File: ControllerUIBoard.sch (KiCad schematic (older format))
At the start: 27 parts, among them J6 ATMEGA_PROG, J7 SignalStrength, J8 UIBoardCON1, Q1 BSS314PEH6327XTSA1, SW1 KeySwitch, U1 ATmega4809-A

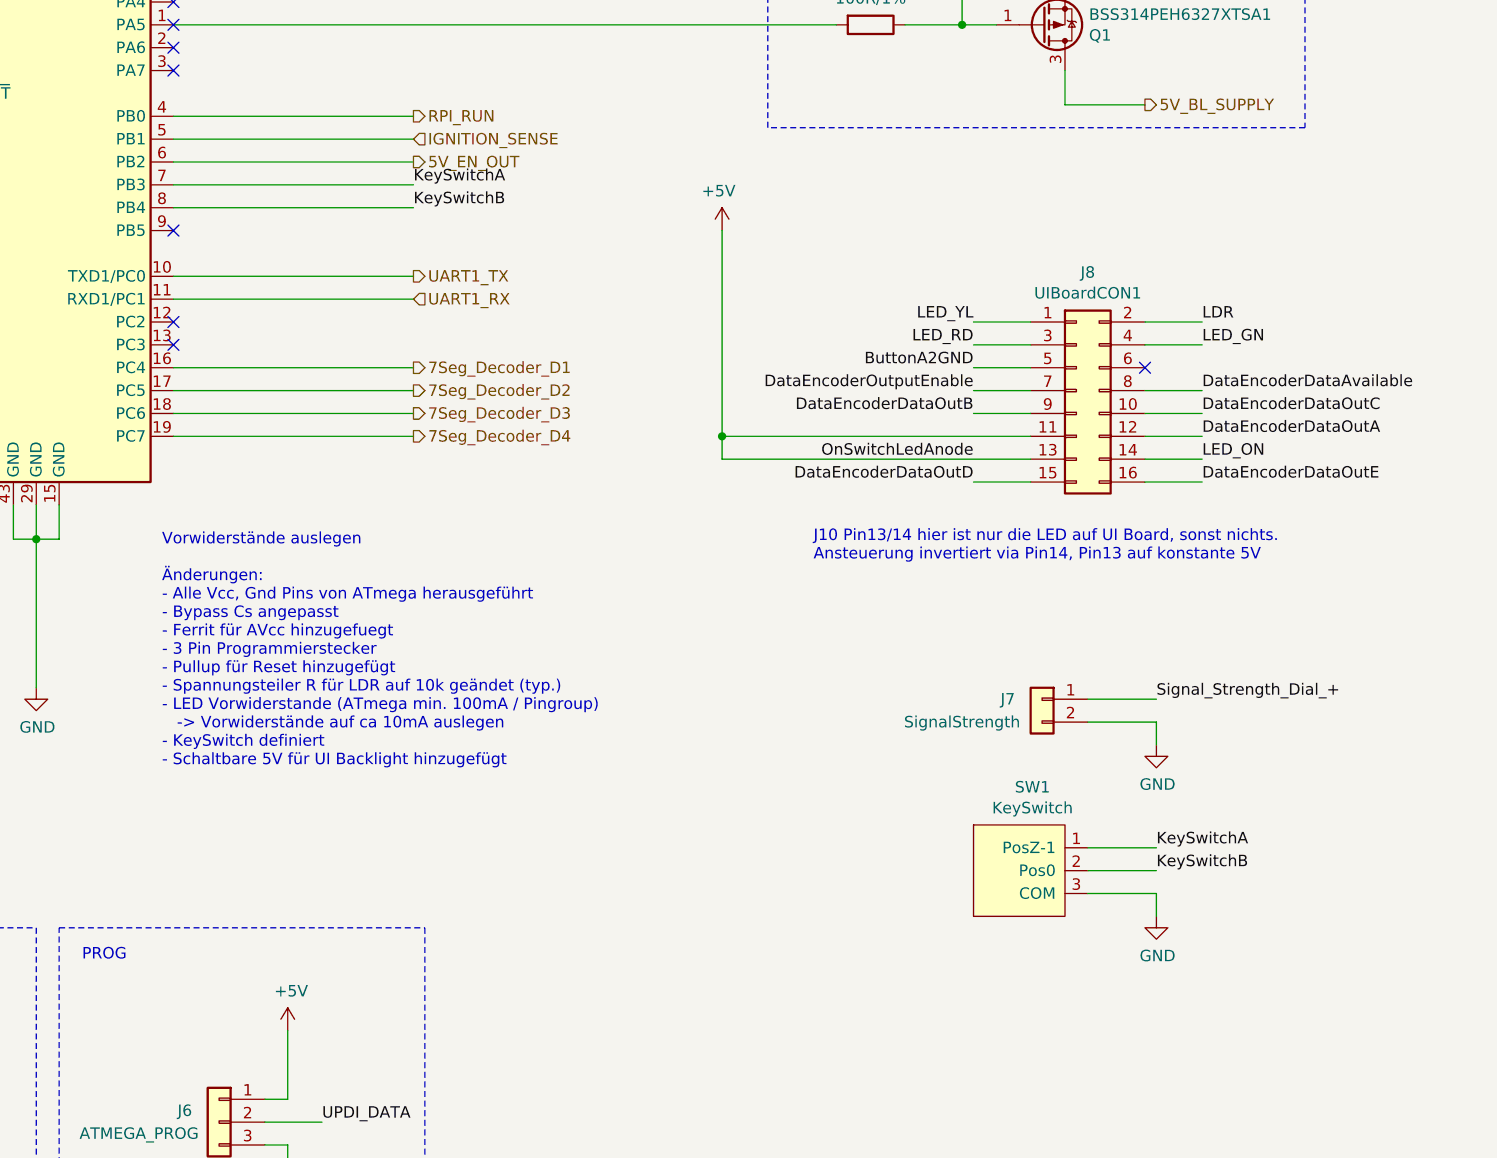
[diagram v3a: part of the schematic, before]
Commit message: - SW1 entfernt
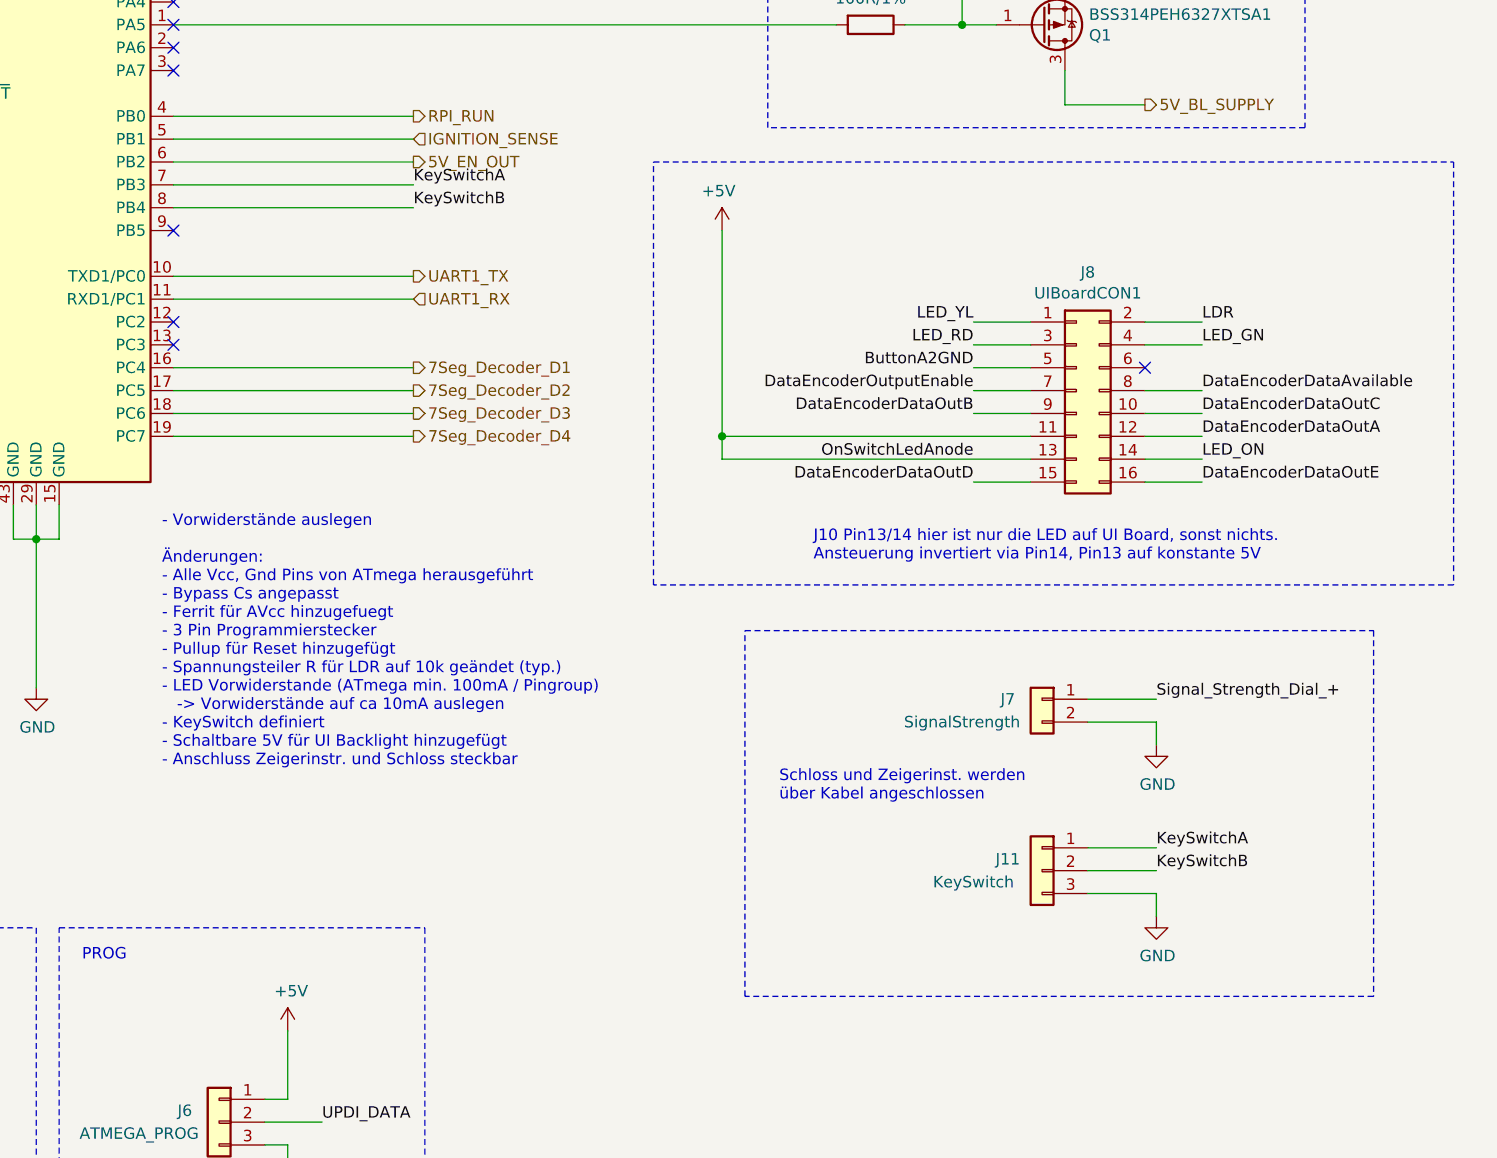
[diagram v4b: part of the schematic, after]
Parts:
- removed SW1: KeySwitch, TeKaDe:KeySwitch, symbol TeKaDe:KeySwitch
- added J11: KeySwitch, Connector_PinHeader_2.54mm:PinHeader_1x03_P2.54mm_Vertical, symbol Connector_Generic:Conn_01x03
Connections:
- net GND: now also J11.3 (Pin_3)
- net KeySwitchA: now also J11.1 (Pin_1)
- net KeySwitchB: now also J11.2 (Pin_2)
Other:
- note added: "- Vorwiderstände auslegen\n\nÄnderungen:\n- Alle Vcc, Gnd Pins von ATmega herausgeführt\n- Bypass Cs angepasst\n- Ferrit für AVcc hinzugefuegt\n- 3 Pin Programmierstecker\n- Pullup für Reset hinzugefügt\n- Spannungsteiler R für LDR auf 10k geändet (typ.)\n- LED Vorwiderstande (ATmega min. 100mA / Pingroup)\n -> Vorwiderstände auf ca 10mA auslegen\n- KeySwitch definiert\n- Schaltbare 5V für UI Bac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"
- note added: "Schloss und Zeigerinst. werden \nüber Kabel angeschlossen"
- note removed: "Vorwiderstände auslegen\n\nÄnderungen:\n- Alle Vcc, Gnd Pins von ATmega herausgeführt\n- Bypass Cs angepasst\n- Ferrit für AVcc hinzugefuegt\n- 3 Pin Programmierstecker\n- Pullup für Reset hinzugefügt\n- Spannungsteiler R für LDR auf 10k geändet (typ.)\n- LED Vorwiderstande (ATmega min. 100mA / Pingroup)\n -> Vorwiderstände auf ca 10mA auslegen\n- KeySwitch definiert\n- Schaltbare 5V für UI Backl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"
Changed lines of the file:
@@
 	4850 1100 4850 1450
 Text Notes 5250 5400 0    50   ~ 0
-Vorwiderstände auslegen\n\nÄnderungen:\n- Alle Vcc, Gnd Pins von ATmega herausgeführt\n- Bypass Cs angepasst\n- Ferrit für AVcc hinzugefuegt\n- 3 Pin Programmierstecker\n- Pullup für Reset hinzugefügt\n- Spannungsteiler R für LDR auf 10k geändet (typ.)\n- LED Vorwiderstande (ATmega min. 100mA / Pingroup)\n   -> Vorwiderstände auf ca 10mA auslegen\n- KeySwitch definiert\n- Schaltbare 5V für UI Backlight hinzugefügt
+- Vorwiderstände auslegen\n\nÄnderungen:\n- Alle Vcc, Gnd Pins von ATmega herausgeführt\n- Bypass Cs angepasst\n- Ferrit für AVcc hinzugefuegt\n- 3 Pin Programmierstecker\n- Pullup für Reset hinzugefügt\n- Spannungsteiler R für LDR auf 10k geändet (typ.)\n- LED Vorwiderstande (ATmega min. 100mA / Pingroup)\n   -> Vorwiderstände auf ca 10mA auslegen\n- KeySwitch definiert\n- Schaltbare 5V für UI Backlight hinzugefügt\n- Anschluss Zeigerinstr. und Schloss steckbar
 $Comp
 L Device:C C?
@@
 	3300 2350 4100 2350
 NoConn ~ 4100 2250
-$Comp
-L TeKaDe:KeySwitch SW1
-U 1 1 614FE351
-P 9300 5750
-F 0 "SW1" H 9058 6015 50  0000 C CNN
-F 1 "KeySwitch" H 9058 5924 50  0000 C CNN
-F 2 "TeKaDe:KeySwitch" H 9350 6200 50  0001 C CNN
-F 3 "" H 9250 5500 50  0001 C CNN
-	1    9300 5750
-	1    0    0    -1
-$EndComp
 Text Notes 8100 4500 0    50   ~ 0
 J10 Pin13/14 hier ist nur die LED auf UI Board, sonst nichts.\nAnsteuerung invertiert via Pin14, Pin13 auf konstante 5V
@@
 Wire Notes Line
 	7900 2600 7900 1150
+$Comp
+L Connector_Generic:Conn_01x03 J11
+U 1 1 6182A98D
+P 9100 5850
+F 0 "J11" H 9250 5900 50  0000 C CNN
+F 1 "KeySwitch" H 9400 5800 50  0000 C CNN
+F 2 "Connector_PinHeader_2.54mm:PinHeader_1x03_P2.54mm_Vertical" H 9100 5850 50  0001 C CNN
+F 3 "~" H 9100 5850 50  0001 C CNN
+	1    9100 5850
+	-1   0    0    -1
+$EndComp
+Wire Notes Line
+	7800 4800 10550 4800
+Wire Notes Line
+	10550 4800 10550 6400
+Wire Notes Line
+	10550 6400 7800 6400
+Wire Notes Line
+	7800 6400 7800 4800
+Text Notes 7950 5550 0    50   ~ 0
+Schloss und Zeigerinst. werden \nüber Kabel angeschlossen
+Wire Notes Line
+	7400 2750 10900 2750
+Wire Notes Line
+	10900 2750 10900 4600
+Wire Notes Line
+	10900 4600 7400 4600
+Wire Notes Line
+	7400 4600 7400 2750
 $EndSCHEMATC

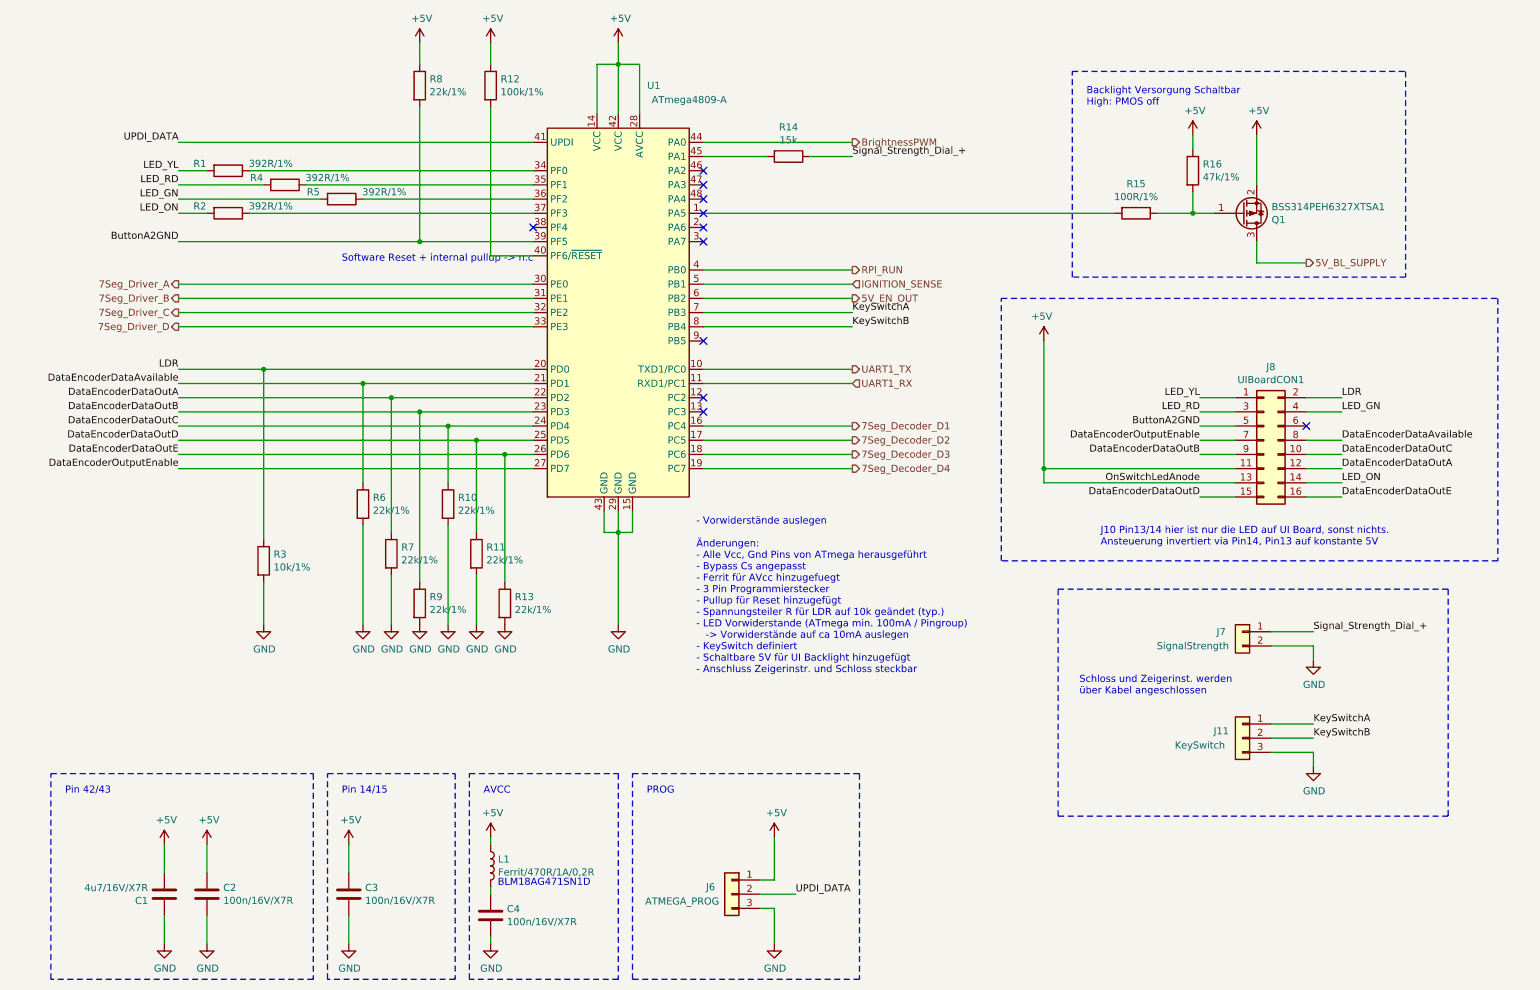
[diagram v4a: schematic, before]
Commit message: - Wert und Footprint der LED Vorwiderstaende angepasst
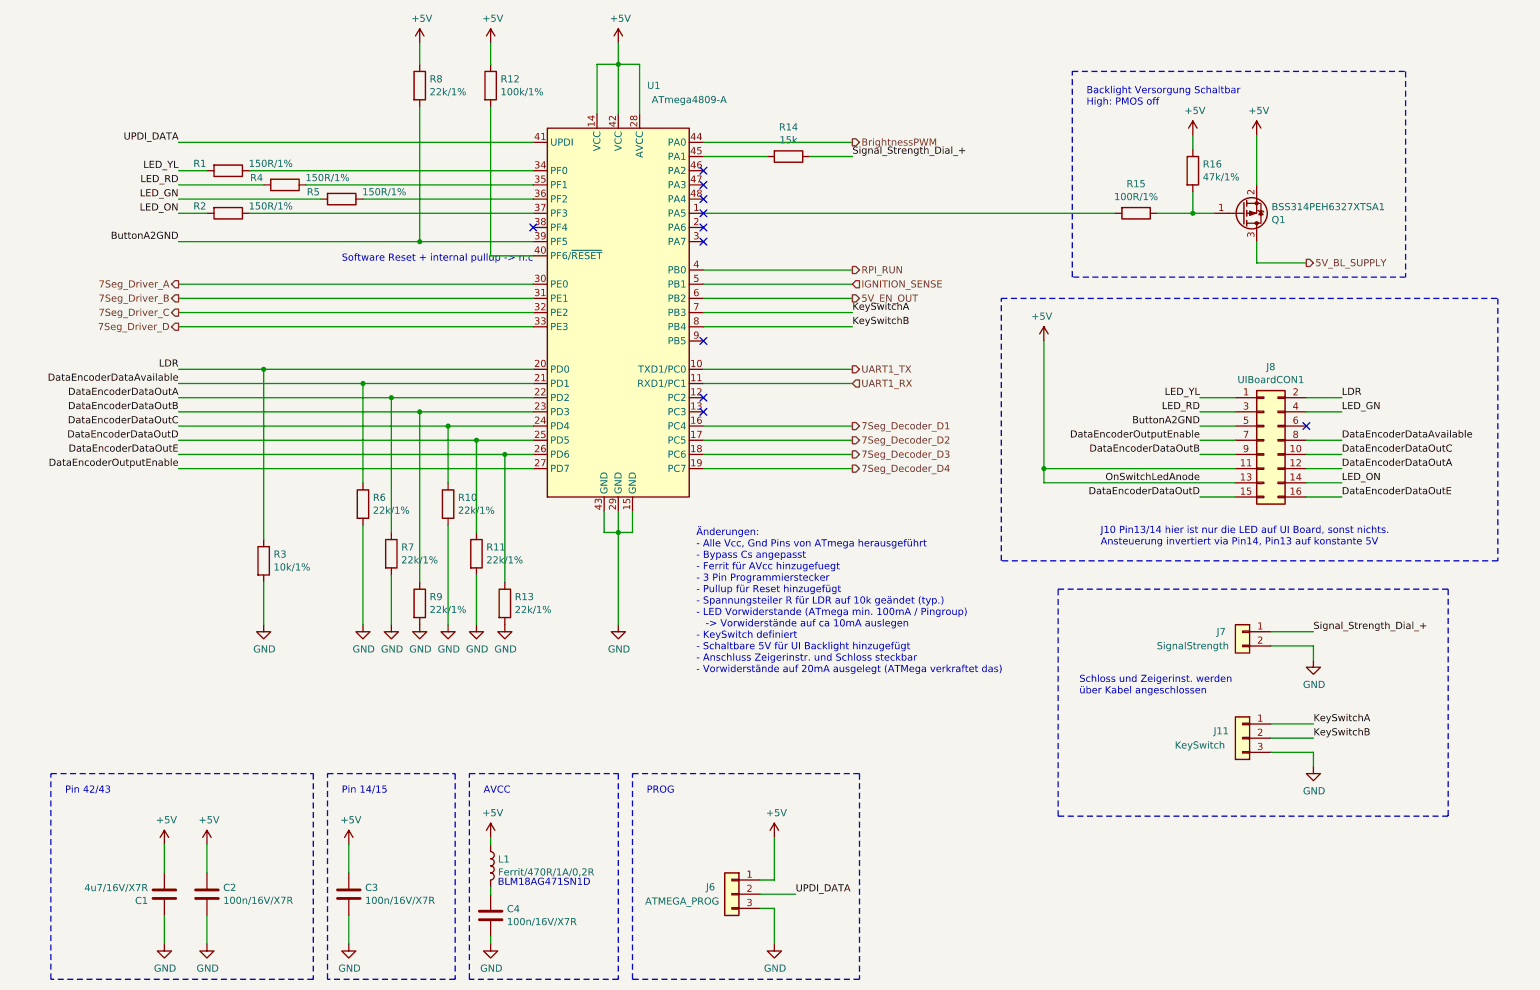
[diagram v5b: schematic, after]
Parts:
- R1, R2, R4, R5: value 392R/1% -> 150R/1%; footprint Resistor_SMD:R_0805_2012Metric -> Resistor_SMD:R_0603_1608Metric
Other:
- note added: "Änderungen:\n- Alle Vcc, Gnd Pins von ATmega herausgeführt\n- Bypass Cs angepasst\n- Ferrit für AVcc hinzugefuegt\n- 3 Pin Programmierstecker\n- Pullup für Reset hinzugefügt\n- Spannungsteiler R für LDR auf 10k geändet (typ.)\n- LED Vorwiderstande (ATmega min. 100mA / Pingroup)\n -> Vorwiderstände auf ca 10mA auslegen\n- KeySwitch definiert\n- Schaltbare 5V für UI Backlight hinzugefügt\n- Anschlu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"
- note removed: "- Vorwiderstände auslegen\n\nÄnderungen:\n- Alle Vcc, Gnd Pins von ATmega herausgeführt\n- Bypass Cs angepasst\n- Ferrit für AVcc hinzugefuegt\n- 3 Pin Programmierstecker\n- Pullup für Reset hinzugefügt\n- Spannungsteiler R für LDR auf 10k geändet (typ.)\n- LED Vorwiderstande (ATmega min. 100mA / Pingroup)\n -> Vorwiderstände auf ca 10mA auslegen\n- KeySwitch definiert\n- Schaltbare 5V für UI Bac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"
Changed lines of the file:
@@
 	4850 1100 4850 1450
 Text Notes 5250 5400 0    50   ~ 0
-- Vorwiderstände auslegen\n\nÄnderungen:\n- Alle Vcc, Gnd Pins von ATmega herausgeführt\n- Bypass Cs angepasst\n- Ferrit für AVcc hinzugefuegt\n- 3 Pin Programmierstecker\n- Pullup für Reset hinzugefügt\n- Spannungsteiler R für LDR auf 10k geändet (typ.)\n- LED Vorwiderstande (ATmega min. 100mA / Pingroup)\n   -> Vorwiderstände auf ca 10mA auslegen\n- KeySwitch definiert\n- Schaltbare 5V für UI Backlight hinzugefügt\n- Anschluss Zeigerinstr. und Schloss steckbar
+Änderungen:\n- Alle Vcc, Gnd Pins von ATmega herausgeführt\n- Bypass Cs angepasst\n- Ferrit für AVcc hinzugefuegt\n- 3 Pin Programmierstecker\n- Pullup für Reset hinzugefügt\n- Spannungsteiler R für LDR auf 10k geändet (typ.)\n- LED Vorwiderstande (ATmega min. 100mA / Pingroup)\n   -> Vorwiderstände auf ca 10mA auslegen\n- KeySwitch definiert\n- Schaltbare 5V für UI Backlight hinzugefügt\n- Anschluss Zeigerinstr. und Schloss steckbar\n- Vorwiderstände auf 20mA ausgelegt (ATMega verkraftet das)
 $Comp
 L Device:C C?
@@
 AR Path="/60F18E7A/6106DF8A" Ref="R1"  Part="1"
 F 0 "R1" V 1900 1650 50  0000 C CNN
-F 1 "392R/1%" V 1900 2150 50  0000 C CNN
-F 2 "Resistor_SMD:R_0805_2012Metric" V 1880 1850 50  0001 C CNN
+F 1 "150R/1%" V 1900 2150 50  0000 C CNN
+F 2 "Resistor_SMD:R_0603_1608Metric" V 1880 1850 50  0001 C CNN
 F 3 "~" H 1950 1850 50  0001 C CNN
 	1    1950 1850
@@
 AR Path="/60F18E7A/6109F54B" Ref="R4"  Part="1"
 F 0 "R4" V 2300 1750 50  0000 C CNN
-F 1 "392R/1%" V 2300 2250 50  0000 C CNN
-F 2 "Resistor_SMD:R_0805_2012Metric" V 2280 1950 50  0001 C CNN
+F 1 "150R/1%" V 2300 2250 50  0000 C CNN
+F 2 "Resistor_SMD:R_0603_1608Metric" V 2280 1950 50  0001 C CNN
 F 3 "~" H 2350 1950 50  0001 C CNN
 	1    2350 1950
@@
 AR Path="/60F18E7A/6109FC15" Ref="R2"  Part="1"
 F 0 "R2" V 1900 1950 50  0000 C CNN
-F 1 "392R/1%" V 1900 2450 50  0000 C CNN
-F 2 "Resistor_SMD:R_0805_2012Metric" V 1880 2150 50  0001 C CNN
+F 1 "150R/1%" V 1900 2450 50  0000 C CNN
+F 2 "Resistor_SMD:R_0603_1608Metric" V 1880 2150 50  0001 C CNN
 F 3 "~" H 1950 2150 50  0001 C CNN
 	1    1950 2150
@@
 AR Path="/60F18E7A/6109F8B5" Ref="R5"  Part="1"
 F 0 "R5" V 2700 1850 50  0000 C CNN
-F 1 "392R/1%" V 2700 2350 50  0000 C CNN
-F 2 "Resistor_SMD:R_0805_2012Metric" V 2680 2050 50  0001 C CNN
+F 1 "150R/1%" V 2700 2350 50  0000 C CNN
+F 2 "Resistor_SMD:R_0603_1608Metric" V 2680 2050 50  0001 C CNN
 F 3 "~" H 2750 2050 50  0001 C CNN
 	1    2750 2050

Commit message: - Steckverbinder Signal und Lock aktualisiert
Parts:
- J11: footprint Connector_PinHeader_2.54mm:PinHeader_1x03_P2.54mm_Vertical -> Connector_Molex:Molex_PicoBlade_53048-0310_1x03_P1.25mm_Horizontal
- J7: footprint Connector_PinHeader_2.54mm:PinHeader_1x02_P2.54mm_Vertical -> Connector_Molex:Molex_PicoBlade_53048-0210_1x02_P1.25mm_Horizontal
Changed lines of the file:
@@
 F 0 "J7" H 9250 5100 50  0000 C CNN
 F 1 "SignalStrength" H 9450 5000 50  0000 C CNN
-F 2 "Connector_PinHeader_2.54mm:PinHeader_1x02_P2.54mm_Vertical" H 9100 5100 50  0001 C CNN
+F 2 "Connector_Molex:Molex_PicoBlade_53048-0210_1x02_P1.25mm_Horizontal" H 9100 5100 50  0001 C CNN
 F 3 "~" H 9100 5100 50  0001 C CNN
 	1    9100 5100
@@
 F 0 "J11" H 9250 5900 50  0000 C CNN
 F 1 "KeySwitch" H 9400 5800 50  0000 C CNN
-F 2 "Connector_PinHeader_2.54mm:PinHeader_1x03_P2.54mm_Vertical" H 9100 5850 50  0001 C CNN
+F 2 "Connector_Molex:Molex_PicoBlade_53048-0310_1x03_P1.25mm_Horizontal" H 9100 5850 50  0001 C CNN
 F 3 "~" H 9100 5850 50  0001 C CNN
 	1    9100 5850
